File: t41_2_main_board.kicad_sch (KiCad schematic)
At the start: 50 parts, among them IC1 74HC125D, J1 Conn_02x08_Odd_Even, J10 SJ-3524-SMT, J11 B2B-XH-A_LF__SN_, J12 SJ-3524-SMT, J13 B3B-XH-A_LF__SN_, J14 B2B-XH-A_LF__SN_, J15 B4B-XH-A_LF__SN_, J16 B3B-XH-A_LF__SN_, J2 Conn_02x05_Odd_Even, J3 Conn_02x05_Odd_Even, J4 Conn_02x05_Odd_Even, J5 Conn_02x05_Odd_Even, J6 SJ-3524-SMT, J7 SJ-3524-SMT, J8 SJ-3524-SMT, J9 B3B-XH-A_LF__SN_, U1 Teensy4.1

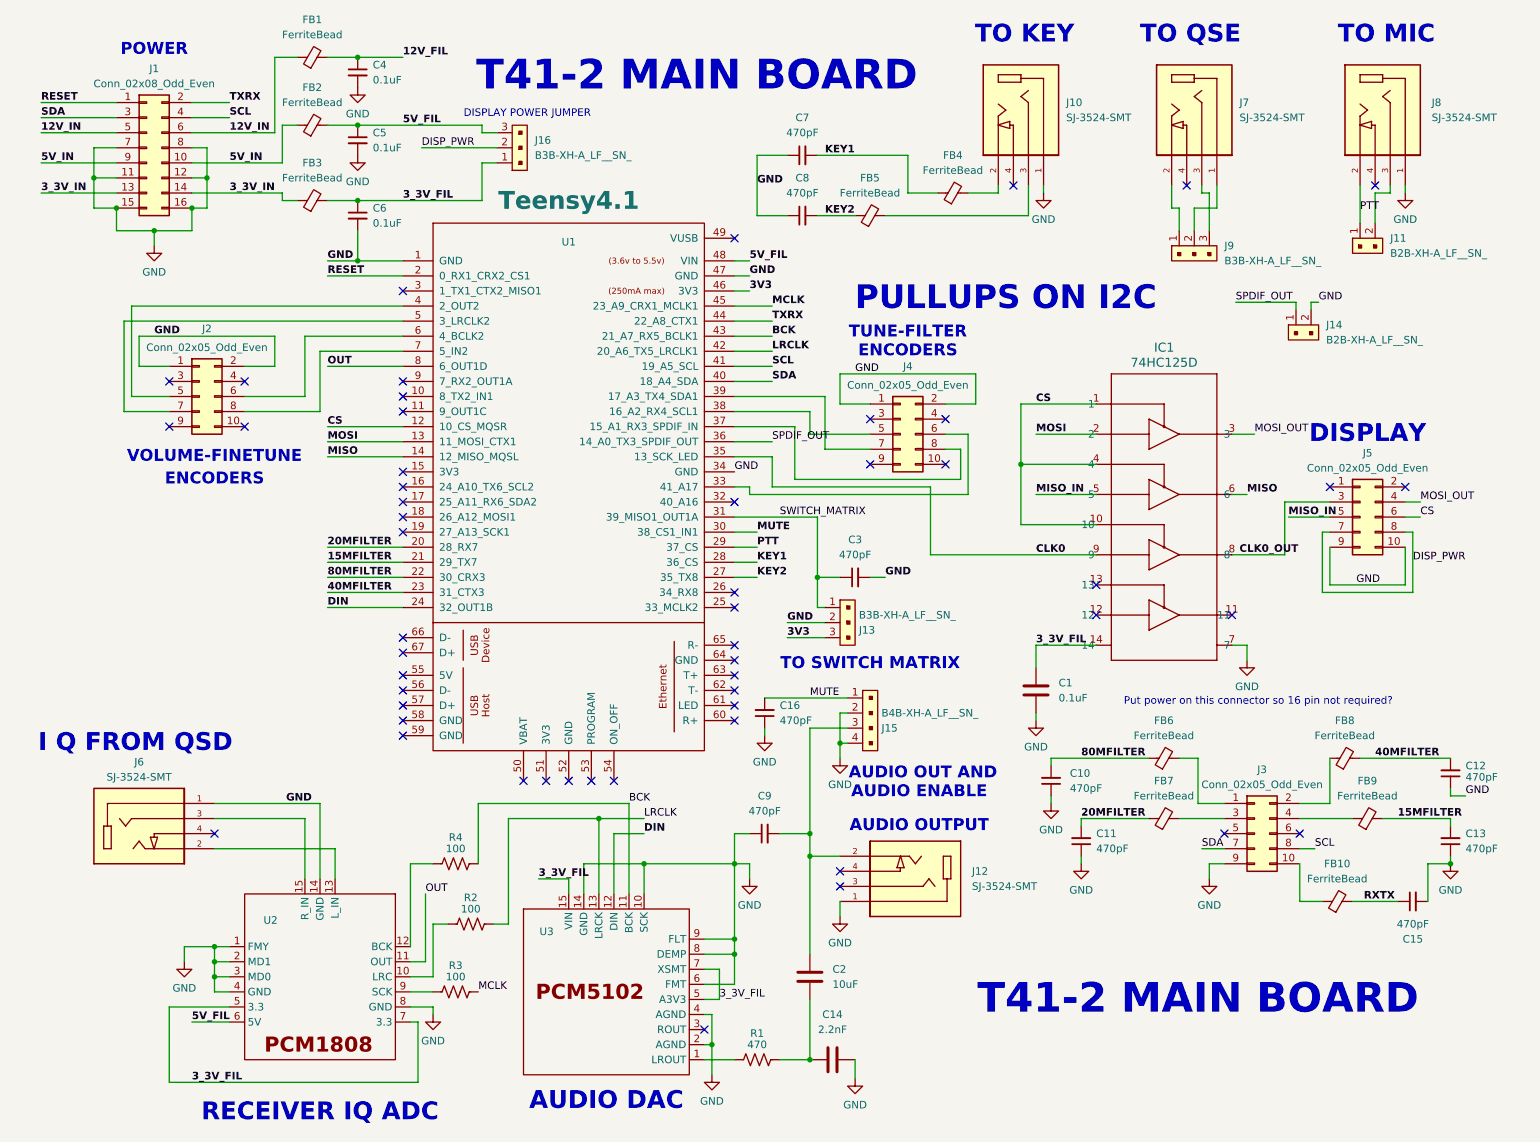
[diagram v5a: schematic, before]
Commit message: V1.1 routes 0.  Needs further clean-up.
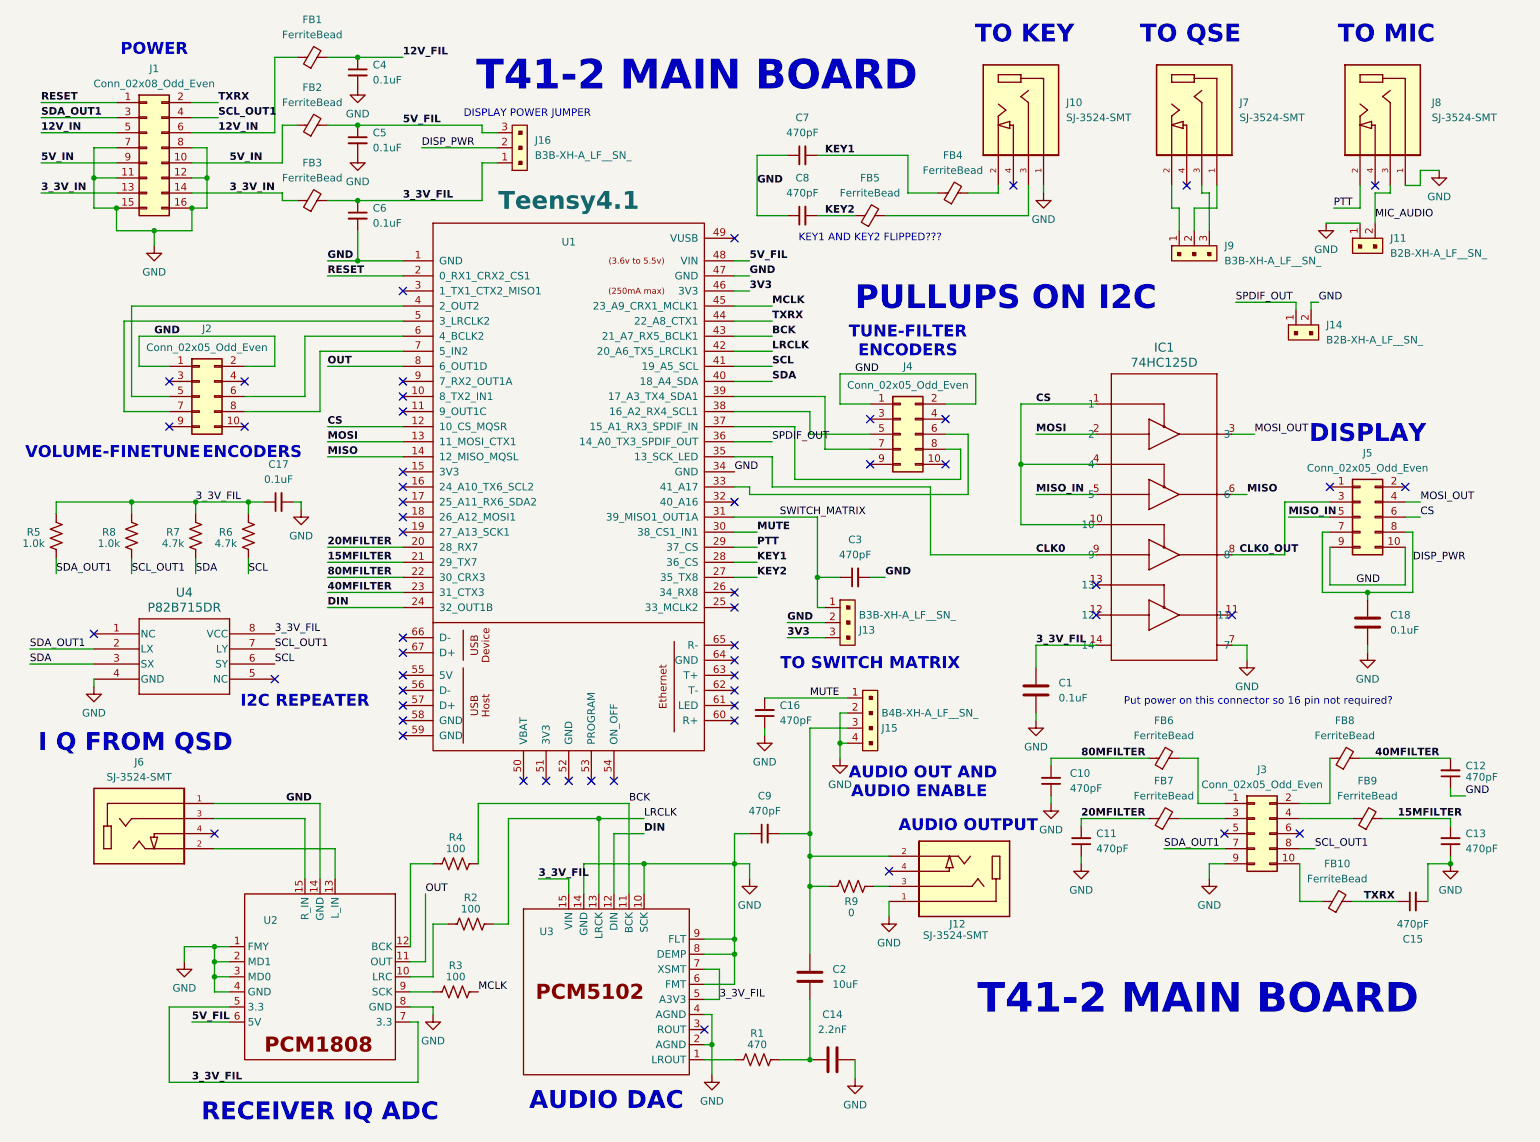
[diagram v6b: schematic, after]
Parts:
- added C17: 0.1uF, Capacitor_SMD:C_1206_3216Metric, symbol Device:C_Small
- added C18: 0.1uF, Capacitor_SMD:C_1206_3216Metric, symbol Device:C
- added R5, R8: 1.0k, Resistor_SMD:R_1206_3216Metric, symbol Device:R_US
- added R6, R7: 4.7k, Resistor_SMD:R_1206_3216Metric, symbol Device:R_US
- added R9: 0, Resistor_SMD:R_1206_3216Metric, symbol Device:R_US
- added U4: P82B715DR, Package_SO:SOIC-8_3.9x4.9mm_P1.27mm, symbol P82B715:P82B715DR
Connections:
- net RXTX is gone; now on net TXRX: C15.1, FB10.2
- net 3_3V_FIL: now also C17.1, R5.2, R6.2, R7.2, R8.2, U4.8 (VCC)
- net DISP_PWR: now also C18.1
- net GND: now also J11.1, C17.2, C18.2, U4.4 (GND)
- net PTT: no longer J11.1
- net SCL: now also R6.1, U4.6 (SY); no longer J1.4 (Pin_4), J3.8 (Pin_8)
- net SDA: now also R7.1, U4.3 (SX); no longer J1.3 (Pin_3), J3.7 (Pin_7)
- net MIC_AUDIO: now reaches J11.2, J8.3
- net at C2.2, C9.2, J12.2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: now also R9.1
- net at J12.3: now also R9.2
- new net SCL_OUT1: J1.4 (Pin_4), J3.8 (Pin_8), R8.1, U4.7 (LY)
- new net SDA_OUT1: J1.3 (Pin_3), J3.7 (Pin_7), R5.1, U4.2 (LX)
- no-connect marks 53 -> 54
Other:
- note added: "I2C REPEATER"
- note added: "KEY1 AND KEY2 FLIPPED???"
- moved on the sheet: J12

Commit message: Fixed schematic route of 3.3 volts and 12 volts to filter connector.
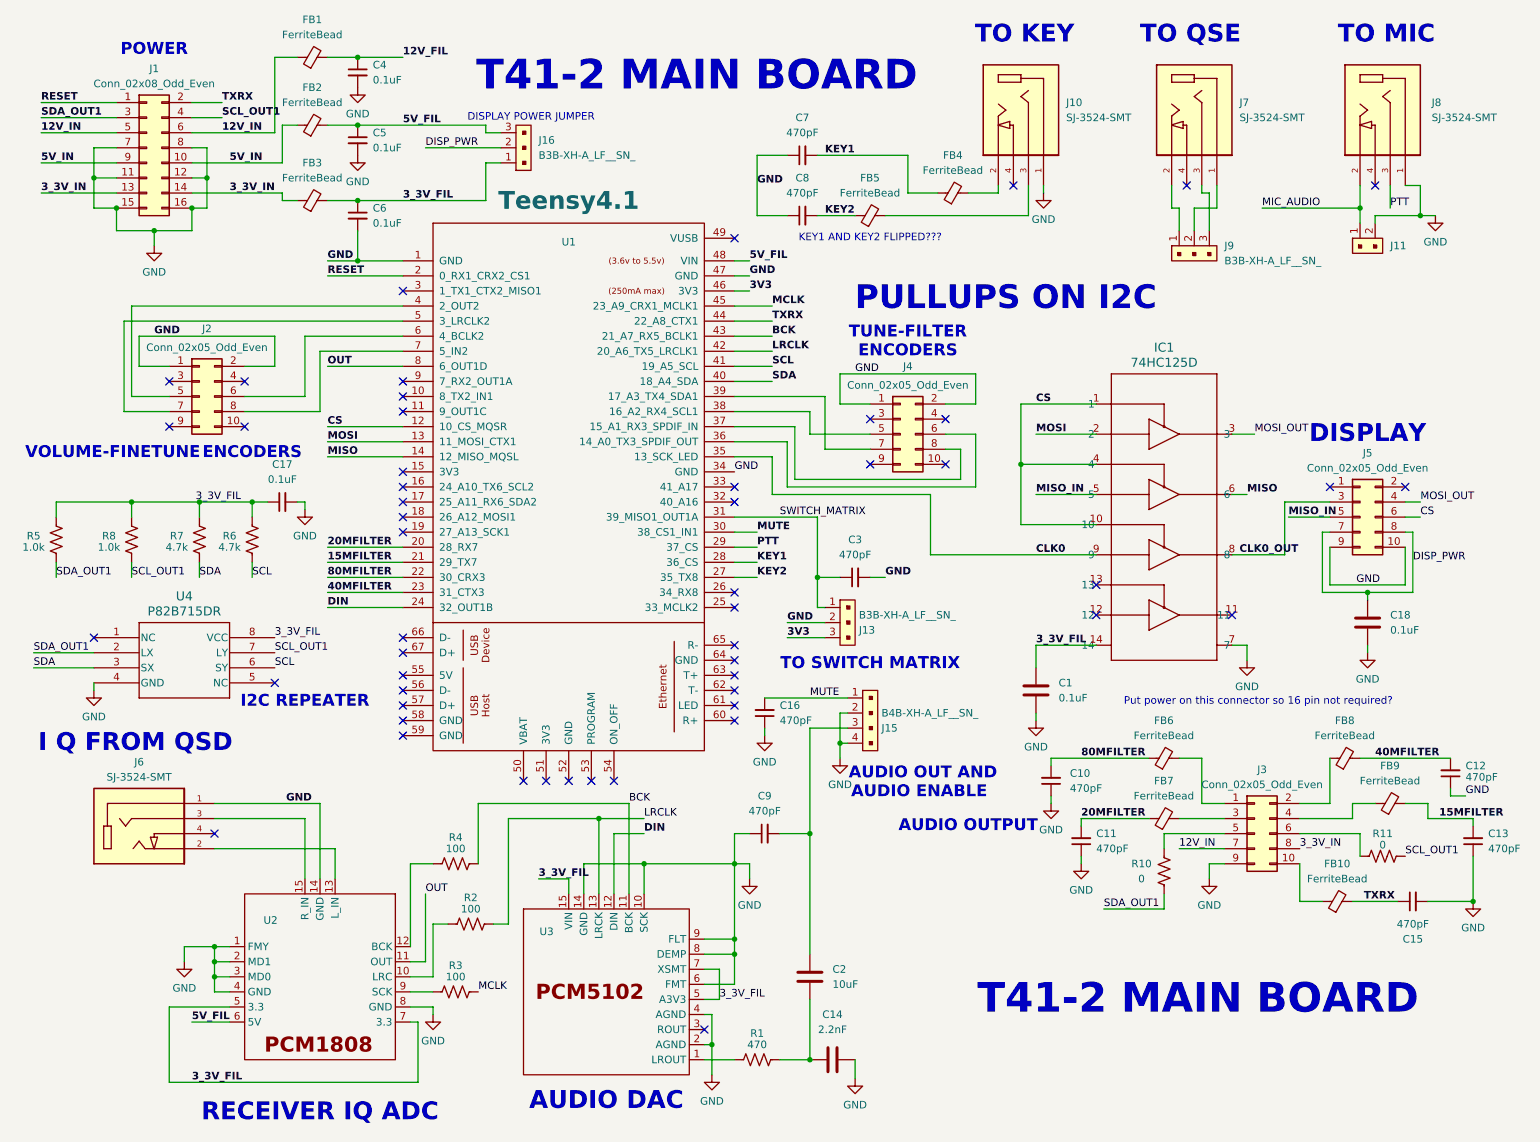
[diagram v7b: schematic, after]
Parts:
- removed J12: SJ-3524-SMT, SJ-3524-SMT:CUI_SJ-3524-SMT, symbol SJ-3524-SMT:SJ-3524-SMT
- removed J14: B2B-XH-A_LF__SN_, digikey-footprints:PinHeader_1x2_P2.5mm_Drill1.1mm, symbol dk_Rectangular-Connectors-Headers-Male-Pins:B2B-XH-A_LF__SN_
- removed R9: 0, Resistor_SMD:R_1206_3216Metric, symbol Device:R_US
- added R10, R11: 0, Resistor_SMD:R_1206_3216Metric, symbol Device:R_US
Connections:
- net SPDIF_OUT is gone; now on an unnamed net: U1.36 (14_A0_TX3_SPDIF_OUT)
- net 12V_IN: now also J3.7 (Pin_7)
- net 3_3V_IN: now also J3.8 (Pin_8)
- net GND: now also J11.2; no longer J11.1
- net MIC_AUDIO: now also J11.1, J8.2; no longer J11.2, J8.3
- net PTT: now also J8.3; no longer J8.2
- net SCL_OUT1: now also R11.2; no longer J3.8 (Pin_8)
- net SDA_OUT1: now also R10.1; no longer J3.7 (Pin_7)
- net at J4.6 (Pin_6): no longer U1.33 (41_A17)
- net at J3.5 (Pin_5): now also R10.2
- net at J3.6 (Pin_6): now also R11.1
- no-connect marks 54 -> 52
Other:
- moved on the sheet: C13, C17, FB9, J16, R5, R6, R7, R8, U4

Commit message: Layout re-do probably done.
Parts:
- added C19: 470pF, Capacitor_SMD:C_1206_3216Metric, symbol Device:C_Small
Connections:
- net GND: now also C19.2
- net TXRX: now also C19.1
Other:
- note added: "LOW PASS FILTER CONTROL"
- note removed: "AUDIO OUTPUT"
- note removed: "KEY1 AND KEY2 FLIPPED???"
- note removed: "PULLUPS ON I2C"
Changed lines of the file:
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@@
 	(title_block
 		(title "T41-2 Main Board")
-		(date "2024-09-17")
+		(date "2024-09-19")
 		(rev "1.2")
 	)
@@
 	(wire
 		(pts
-			(xy 226.06 96.52) (xy 233.68 96.52)
-		)
-		(stroke
-			(width 0)
-			(type default)
-		)
-	)
-	(wire
-		(pts
 			(xy 31.75 96.52) (xy 43.18 96.52)
 		)
@@
 	(wire
 		(pts
+			(xy 226.06 99.06) (xy 233.68 99.06)
+		)
+		(stroke
+			(width 0)
+			(type default)
+		)
+	)
+	(wire
+		(pts
 			(xy 107.95 162.56) (xy 107.95 157.48)
 		)
@@
 	(wire
 		(pts
-			(xy 140.97 190.5) (xy 146.05 190.5)
+			(xy 217.17 105.41) (xy 224.79 105.41)
 		)
 		(stroke
@@
 	(wire
 		(pts
-			(xy 217.17 105.41) (xy 226.06 105.41)
+			(xy 140.97 190.5) (xy 146.05 190.5)
 		)
 		(stroke
@@
 	(wire
 		(pts
+			(xy 158.75 59.69) (xy 161.29 59.69)
+		)
+		(stroke
+			(width 0)
+			(type default)
+		)
+	)
+	(wire
+		(pts
 			(xy 214.63 46.99) (xy 214.63 43.18)
 		)
@@
 	(wire
 		(pts
+			(xy 149.86 59.69) (xy 149.86 66.04)
+		)
+		(stroke
+			(width 0)
+			(type default)
+		)
+	)
+	(wire
+		(pts
 			(xy 64.77 58.42) (xy 77.47 58.42)
 		)
@@
 	(wire
 		(pts
+			(xy 224.79 96.52) (xy 224.79 105.41)
+		)
+		(stroke
+			(width 0)
+			(type default)
+		)
+	)
+	(wire
+		(pts
 			(xy 173.99 74.93) (xy 173.99 80.01)
 		)
@@
 	(wire
 		(pts
-			(xy 133.35 66.04) (xy 139.7 66.04)
+			(xy 133.35 66.04) (xy 149.86 66.04)
 		)
 		(stroke
@@
 	(wire
 		(pts
-			(xy 226.06 105.41) (xy 226.06 96.52)
-		)
-		(stroke
-			(width 0)
-			(type default)
-		)
-	)
-	(wire
-		(pts
 			(xy 147.32 48.26) (xy 153.67 48.26)
 		)
@@
 	(wire
 		(pts
-			(xy 153.67 190.5) (xy 153.67 193.675)
+			(xy 153.67 190.5) (xy 153.67 194.31)
 		)
 		(stroke
@@
 	(wire
 		(pts
+			(xy 149.86 59.69) (xy 153.67 59.69)
+		)
+		(stroke
+			(width 0)
+			(type default)
+		)
+	)
+	(wire
+		(pts
 			(xy 147.32 38.1) (xy 162.56 38.1)
 		)
@@
 	(wire
 		(pts
-			(xy 226.695 99.06) (xy 233.68 99.06)
-		)
-		(stroke
-			(width 0)
-			(type default)
-		)
-	)
-	(wire
-		(pts
 			(xy 213.36 44.45) (xy 213.36 50.8)
 		)
@@
 	(wire
 		(pts
+			(xy 224.79 96.52) (xy 233.68 96.52)
+		)
+		(stroke
+			(width 0)
+			(type default)
+		)
+	)
+	(wire
+		(pts
 			(xy 177.8 43.18) (xy 177.8 44.45)
 		)
@@
 		)
 	)
-	(text "AUDIO OUTPUT"
-		(exclude_from_sim no)
-		(at 172.72 151.13 0)
-		(effects
-			(font
-				(size 2 2)
-				(thickness 0.4)
-				(bold yes)
-			)
-		)
-	)
 	(text "TO KEY"
 		(exclude_from_sim no)
@@
 		)
 	)
-	(text "KEY1 AND KEY2 FLIPPED???"
-		(exclude_from_sim no)
-		(at 156.21 52.07 0)
-		(effects
-			(font
-				(size 1.27 1.27)
-			)
-		)
-	)
 	(text "T41-2 MAIN BOARD"
 		(exclude_from_sim no)
@@
 		)
 	)
-	(text "PULLUPS ON I2C"
-		(exclude_from_sim no)
-		(at 179.07 62.23 0)
-		(effects
-			(font
-				(size 4 4)
-				(thickness 0.8)
-				(bold yes)
-			)
-		)
-	)
 	(text "AUDIO ENABLE"
 		(exclude_from_sim no)
@@
 		)
 	)
+	(text "LOW PASS FILTER CONTROL"
+		(exclude_from_sim no)
+		(at 220.98 167.64 0)
+		(effects
+			(font
+				(size 2 2)
+				(thickness 0.4)
+				(bold yes)
+			)
+		)
+	)
 	(label "SCL"
 		(at 55.88 124.46 0)
@@
 	)
 	(label "MISO_IN"
-		(at 226.695 99.06 0)
+		(at 226.06 99.06 0)
 		(fields_autoplaced yes)
 		(effects
@@
 	(symbol
 		(lib_id "power:GND")
-		(at 153.67 193.675 0)
+		(at 153.67 194.31 0)
 		(unit 1)
 		(exclude_from_sim no)
@@
 		(fields_autoplaced yes)
 		(property "Reference" "#PWR016"
-			(at 153.67 200.025 0)
+			(at 153.67 200.66 0)
 			(effects
 				(font
@@
 		)
 		(property "Value" "GND"
-			(at 153.67 198.12 0)
+			(at 153.67 198.755 0)
 			(effects
 				(font
@@
 		)
 		(property "Footprint" ""
-			(at 153.67 193.675 0)
+			(at 153.67 194.31 0)
 			(effects
 				(font
@@
 		)
 		(property "Datasheet" ""
-			(at 153.67 193.675 0)
+			(at 153.67 194.31 0)
 			(effects
 				(font
@@
 		)
 		(property "Description" "Power symbol creates a global label with name \"GND\" , ground"
-			(at 153.67 193.675 0)
+			(at 153.67 194.31 0)
 			(effects
 				(font
@@
 	)
 	(symbol
+		(lib_id "Device:C_Small")
+		(at 156.21 59.69 90)
+		(unit 1)
+		(exclude_from_sim no)
+		(in_bom yes)
+		(on_board yes)
+		(dnp no)
+		(property "Reference" "C19"
+			(at 156.21 54.61 90)
+			(effects
+				(font
+					(size 1.27 1.27)
+				)
+			)
+		)
+		(property "Value" "470pF"
+			(at 156.21 57.15 90)
+			(effects
+				(font
+					(size 1.27 1.27)
+				)
+			)
+		)
+		(property "Footprint" "Capacitor_SMD:C_1206_3216Metric"
+			(at 156.21 59.69 0)
+			(effects
+				(font
+					(size 1.27 1.27)
+				)
+				(hide yes)
+			)
+		)
+		(property "Datasheet" "~"
+			(at 156.21 59.69 0)
+			(effects
+				(font
+					(size 1.27 1.27)
+				)
+				(hide yes)
+			)
+		)
+		(property "Description" "Unpolarized capacitor, small symbol"
+			(at 156.21 59.69 0)
+			(effects
+				(font
+					(size 1.27 1.27)
+				)
+				(hide yes)
+			)
+		)
+		(pin "2"
+		)
+		(pin "1"
+		)
+		(instances
+			(project "t41_2_main_board"
+				(path "/f916f150-4745-4a5f-98ae-b103f17eec30"
+					(reference "C19")
+					(unit 1)
+				)
+			)
+		)
+	)
+	(symbol
 		(lib_id "dk_Rectangular-Connectors-Headers-Male-Pins:B3B-XH-A_LF__SN_")
 		(at 208.28 53.34 0)
@@
 					(unit 1)
 				)
+			)
+		)
+	)
+	(symbol
+		(lib_id "power:GND")
+		(at 161.29 59.69 0)
+		(unit 1)
+		(exclude_from_sim no)
+		(in_bom yes)
+		(on_board yes)
+		(dnp no)
+		(fields_autoplaced yes)
+		(property "Reference" "#PWR011"
+			(at 161.29 66.04 0)
+			(effects
+				(font
+					(size 1.27 1.27)
+				)
+				(hide yes)
+			)
+		)
+		(property "Value" "GND"
+			(at 161.29 64.135 0)
+			(effects
+				(font
+					(size 1.27 1.27)
+				)
+			)
+		)
+		(property "Footprint" ""
+			(at 161.29 59.69 0)
+			(effects
+				(font
+					(size 1.27 1.27)
+				)
+				(hide yes)
+			)
+		)
+		(property "Datasheet" ""
+			(at 161.29 59.69 0)
+			(effects
+				(font
+					(size 1.27 1.27)
+				)
+				(hide yes)
+			)
+		)
+		(property "Description" "Power symbol creates a global label with name \"GND\" , ground"
+			(at 161.29 59.69 0)
+			(effects
+				(font
+					(size 1.27 1.27)
+				)
+				(hide yes)
+			)
+		)
+		(pin "1"
+		)
+		(instances
+			(project "t41_2_main_board"
+				(path "/f916f150-4745-4a5f-98ae-b103f17eec30"
+					(reference "#PWR011")
+					(unit 1)
+				)
